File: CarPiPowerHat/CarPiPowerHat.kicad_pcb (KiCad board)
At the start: 4 copper layers, 65 x 56 mm, 18 parts, among them J3 40HAT, J6 CONN_02X02, J9 CONN_01X02, Q1 DMG2305UX, Q2 DMMT5401, U2 CAT24C32

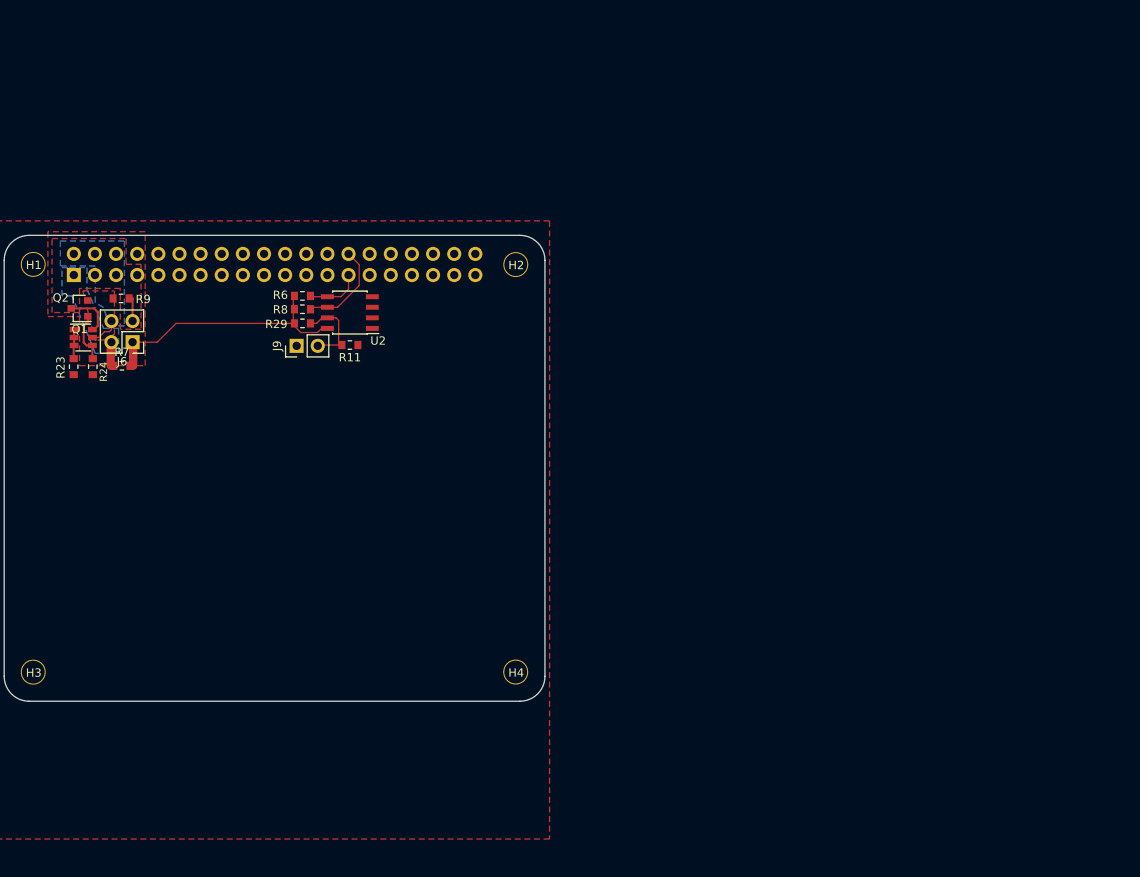
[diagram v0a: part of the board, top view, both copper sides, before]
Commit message: Added first firmware version
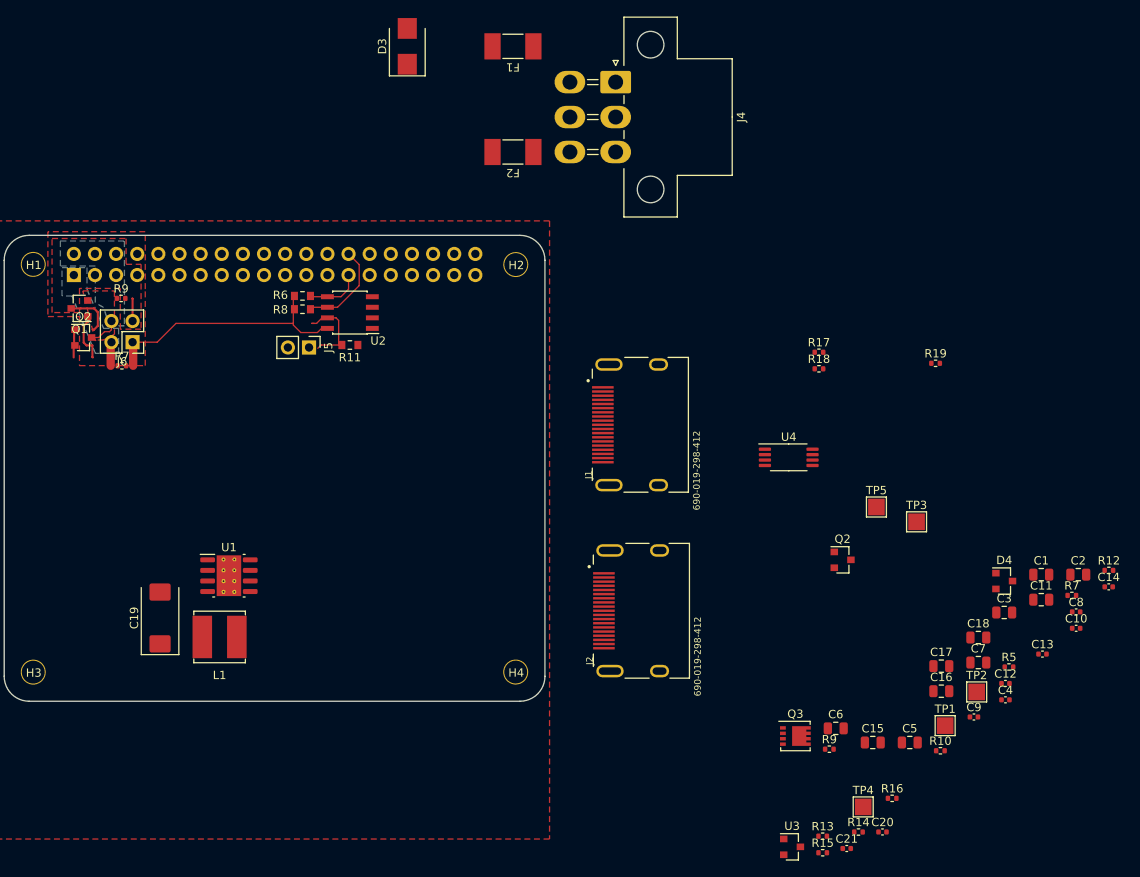
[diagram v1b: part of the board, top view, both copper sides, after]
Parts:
- removed J9: CONN_01X02, Connector_PinHeader_2.54mm:PinHeader_1x02_P2.54mm_Vertical
- removed R23, R29: 10K, Resistor_SMD:R_0603_1608Metric_Pad0.84x1.00mm_HandSolder
- removed R24: 47K, Resistor_SMD:R_0603_1608Metric_Pad0.84x1.00mm_HandSolder
- added C1: 10u 35v, Capacitor_SMD:C_0805_2012Metric, F.Cu at (203.2, 101.6)
- added C10: 100n, Capacitor_SMD:C_0402_1005Metric, F.Cu at (207.4, 108.0)
- added C11: 10u 35v, Capacitor_SMD:C_0805_2012Metric, F.Cu at (203.2, 104.6)
- added C12: nf, Capacitor_SMD:C_0402_1005Metric, F.Cu at (198.9, 114.7)
- added C13: 1.2nF, Capacitor_SMD:C_0402_1005Metric, F.Cu at (203.3, 111.2)
- added C14: nf, Capacitor_SMD:C_0402_1005Metric, F.Cu at (211.3, 103.1)
- added C15: 10u, Capacitor_SMD:C_0805_2012Metric, F.Cu at (182.9, 121.8)
- added C16: 10u, Capacitor_SMD:C_0805_2012Metric, F.Cu at (191.2, 115.6)
- added C17: 10u, Capacitor_SMD:C_0805_2012Metric, F.Cu at (191.2, 112.6)
- added C18: 10u, Capacitor_SMD:C_0805_2012Metric, F.Cu at (195.6, 109.2)
- added C19: 100uF, Capacitor_Tantalum_SMD:CP_EIA-7343-31_Kemet-D, F.Cu at (97.3, 106.8)
- added C2: 10u 35v, Capacitor_SMD:C_0805_2012Metric, F.Cu at (207.7, 101.6)
- added C20: 100n, Capacitor_SMD:C_0402_1005Metric, F.Cu at (184.1, 132.5)
- added C21: 100n, Capacitor_SMD:C_0402_1005Metric, F.Cu at (179.8, 134.5)
- added C3: 10u 35v, Capacitor_SMD:C_0805_2012Metric, F.Cu at (198.8, 106.2)
- added C4: 100n 100v, Capacitor_SMD:C_0402_1005Metric, F.Cu at (198.9, 116.7)
- added C5: 10u 35v, Capacitor_SMD:C_0805_2012Metric, F.Cu at (187.4, 121.8)
- added C6: 10u 35v, Capacitor_SMD:C_0805_2012Metric, F.Cu at (178.5, 120.1)
- added C7: 10u 35v, Capacitor_SMD:C_0805_2012Metric, F.Cu at (195.6, 112.2)
- added C8: 100n, Capacitor_SMD:C_0402_1005Metric, F.Cu at (207.4, 106.1)
- added C9: 100n, Capacitor_SMD:C_0402_1005Metric, F.Cu at (195.1, 118.7)
- added D3: D_TVS, Diode_SMD:D_SMB, F.Cu at (127.0, 38.1)
- added D4: MMBZ5242BLT3G, Diode_SMD:D_SOT-23_ANK, F.Cu at (198.8, 102.4)
- added F1: Fuse, Fuse:Fuse_Littelfuse-NANO2-451_453, F.Cu at (139.7, 38.1)
- added F2: Fuse, Fuse:Fuse_Littelfuse-NANO2-451_453, F.Cu at (139.7, 50.8)
- added J1: 690-019-298-412, project_footprints:EDAC 690-019-298-412, F.Cu at (151.2, 83.6)
- added J2: 690-019-298-412, project_footprints:EDAC 690-019-298-412, F.Cu at (151.4, 105.9)
- added J4: Conn_02x03_Counter_Clockwise, Connector_Molex:Molex_Mini-Fit_Jr_5569-06A1_2x03_P4.20mm_Horizontal, F.Cu at (152.0, 42.4)
- added J5: CONN_01X02, Connector_PinHeader_2.54mm:PinHeader_1x02_P2.54mm_Vertical, F.Cu at (115.2, 74.3)
- added L1: SRN6045TA-3R3Y, Inductor_SMD:L_Bourns_SRN6045TA, F.Cu at (104.4, 109.1)
- added Q2: DMG2305UX, Package_TO_SOT_SMD:SOT-23, F.Cu at (179.3, 99.8)
- added Q3: DMP3013SFV-7, Package_SON:Diodes_PowerDI3333-8, F.Cu at (173.7, 121.0)
- added R10: 12K 1%, Resistor_SMD:R_0402_1005Metric, F.Cu at (191.1, 122.8)
- added R12: 2.2K 1%, Resistor_SMD:R_0402_1005Metric, F.Cu at (211.3, 101.1)
- added R13: 10K 1%, Resistor_SMD:R_0402_1005Metric, F.Cu at (176.9, 133.0)
- added R14: 10K 1%, Resistor_SMD:R_0402_1005Metric, F.Cu at (181.2, 132.5)
- added R15: 10K 1%, Resistor_SMD:R_0402_1005Metric, F.Cu at (176.9, 135.0)
- added R16: 10K 1%, Resistor_SMD:R_0402_1005Metric, F.Cu at (185.3, 128.5)
- added R17: 10K 1%, Resistor_SMD:R_0402_1005Metric, F.Cu at (176.5, 74.9)
- added R18: 320 1%, Resistor_SMD:R_0402_1005Metric, F.Cu at (176.5, 76.9)
- added R19: 3.3K 1%, Resistor_SMD:R_0402_1005Metric, F.Cu at (190.5, 76.2)
- added R5: 12K 1%, Resistor_SMD:R_0402_1005Metric, F.Cu at (199.3, 112.7)
- added R7: 10R, Resistor_SMD:R_0402_1005Metric, F.Cu at (206.9, 104.1)
- added R9: 20K 1%, Resistor_SMD:R_0402_1005Metric, F.Cu at (177.7, 122.6)
- added TP1: TestPoint, TestPoint:TestPoint_Pad_2.0x2.0mm, F.Cu at (191.7, 119.8)
- added TP2: TestPoint, TestPoint:TestPoint_Pad_2.0x2.0mm, F.Cu at (195.4, 115.7)
- added TP3: TestPoint, TestPoint:TestPoint_Pad_2.0x2.0mm, F.Cu at (188.2, 95.2)
- added TP4: TestPoint, TestPoint:TestPoint_Pad_2.0x2.0mm, F.Cu at (181.8, 129.5)
- added TP5: TestPoint, TestPoint:TestPoint_Pad_2.0x2.0mm, F.Cu at (183.4, 93.5)
- added U1: AP64501SP-13, Package_SO:SOIC-8-1EP_3.9x4.9mm_P1.27mm_EP2.95x4.9mm_Mask2.71x3.4mm_ThermalVias, F.Cu at (105.6, 101.7)
- added U3: LM3480-5.0, Package_TO_SOT_SMD:SOT-23, F.Cu at (173.2, 134.3)
- added U4: ATtiny45V-10X, Package_SO:TSSOP-8_4.4x3mm_P0.65mm, F.Cu at (172.8, 87.5)
- J6: value CONN_02X02 -> Conn_01x15_Female
- Q1: value DMG2305UX -> DMMT5401
- Q2: value DMMT5401 -> DMG2305UX; footprint Package_TO_SOT_SMD:SOT-23-6 -> Package_TO_SOT_SMD:SOT-23
- R11: value DNP -> 130
- R7: value DNP -> 10R; footprint Resistor_SMD:R_0603_1608Metric_Pad0.84x1.00mm_HandSolder -> Resistor_SMD:R_0402_1005Metric
- R9: value DNP -> 20K 1%; footprint Resistor_SMD:R_0603_1608Metric_Pad0.84x1.00mm_HandSolder -> Resistor_SMD:R_0402_1005Metric
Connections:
- J3 pad 1: /P3V3_HAT -> /+3.3v
- J3 pad 16: unconnected-(J3-Pad16) -> PWR_SENSE_OUT
- J3 pad 17: unconnected-(J3-Pad17) -> /+3.3v
- J3 pad 18: unconnected-(J3-Pad18) -> PWR_SENSE_IN
- J3 pad 22: unconnected-(J3-Pad22) -> REVERSE_SENSE
- J3 pad 24: unconnected-(J3-Pad24) -> LIGHT_SENSE
- J6 pad 1: /P3V3 -> Net-(J1-Pad15)
- J6 pad 2: /P3V3_HAT -> Net-(J1-Pad14)
- J6 pad 3: /P5V -> Net-(J1-Pad13)
- J6 pad 4: /P5V_HAT -> Net-(J1-Pad1)
- Q1 pad 2: /P5V_HAT -> Net-(Q1-Pad1)
- Q1 pad 3: /P5V -> Net-(Q1-Pad1)
- Q2 pad 1: Net-(Q2-Pad1) -> Net-(Q1-Pad4)
- Q2 pad 2: Net-(Q2-Pad1) -> /P5V_HAT
- Q2 pad 3: Net-(Q2-Pad1) -> /PSU/P5V
- R11 pad 1: Net-(J9-Pad2) -> Net-(D1-Pad1)
- R7 pad 1: /P3V3_HAT -> Net-(L1-Pad1)
- R7 pad 2: /P3V3 -> Net-(C8-Pad1)
- R9 pad 1: /P5V_HAT -> Net-(C12-Pad1)
- R9 pad 2: /P5V -> Net-(C13-Pad1)
- U2 pad 7: Net-(J9-Pad2) -> Net-(J5-Pad2)
- U2 pad 8: /P3V3 -> /+3.3v
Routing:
- net Net-(J9-Pad2): track 9.58 -> 0.00 mm
- net Net-(D1-Pad1): track 0.00 -> 9.58 mm
- net /P5V: track 8.71 -> 0.00 mm
- net Net-(Q1-Pad1): track 6.02 -> 12.0 mm
- net /P5V_HAT: track 3.77 -> 0.00 mm
- net Net-(J1-Pad1): track 0.00 -> 3.72 mm
- net Net-(Q2-Pad1): track 3.37 -> 0.00 mm
- net Net-(C21-Pad1): track 0.00 -> 3.37 mm
- net Net-(J1-Pad14): track 0.00 -> 2.88 mm
- net /P3V3_HAT: track 2.88 -> 0.00 mm
- net Net-(J1-Pad13): track 0.00 -> 2.73 mm
- added copper zone on B.Cu, net /+3.3v
- added copper zone on F.Cu, net Net-(C13-Pad1)
- removed copper zone on B.Cu, net /P3V3_HAT
- removed copper zone on F.Cu, net /P5V
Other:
- board text removed: "This is a HAT compatible PCB starting design based on the official Raspberry Pi specs at: https://github.com/raspberrypi/hats/blob/master/designguide.md Currently the camera slot and display cutout are not here. See the schematic for the details on the EEPROM and power setup. This board does have the correct components for powering the Pi via the HAT. If you need the Pi to provide 5V or 3.3V, ple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"

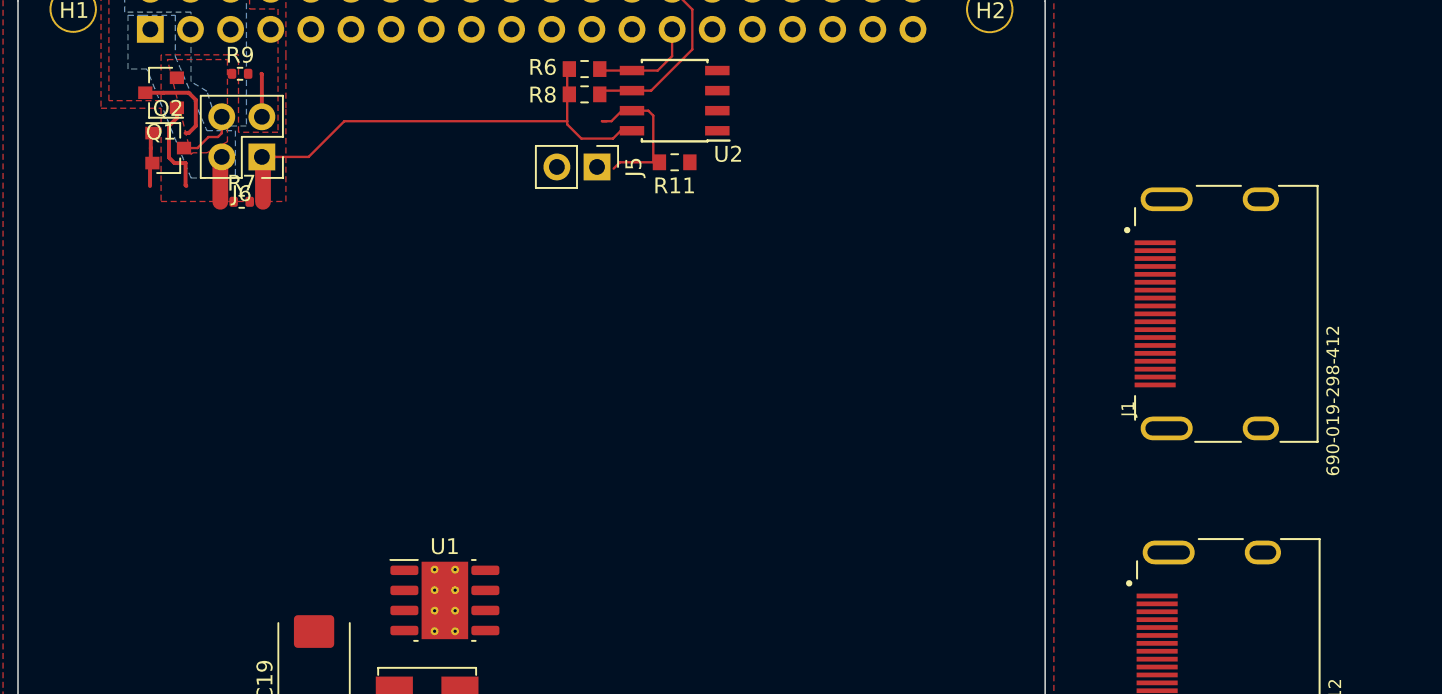
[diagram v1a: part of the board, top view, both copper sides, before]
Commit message: added connectors
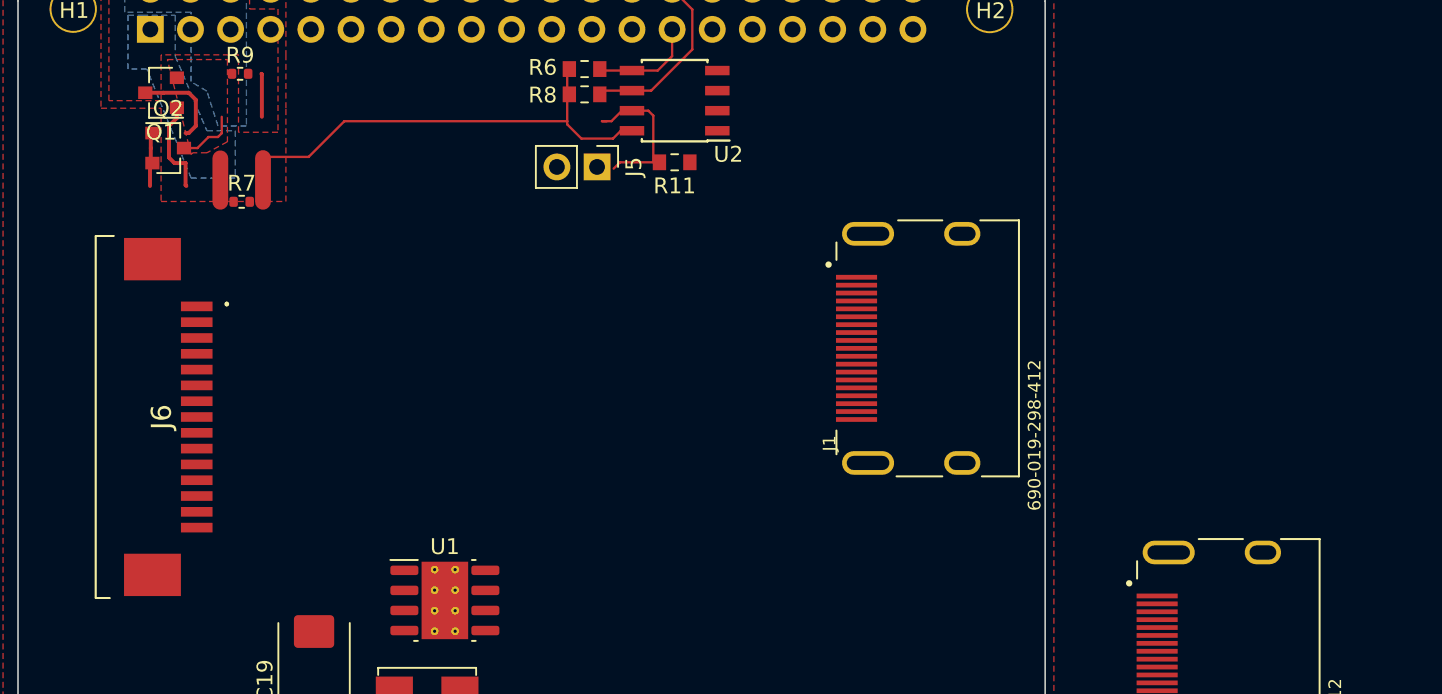
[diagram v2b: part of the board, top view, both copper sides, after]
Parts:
- J6: value Conn_01x15_Female -> 1-84953-5; footprint Connector_PinHeader_2.54mm:PinHeader_2x02_P2.54mm_Vertical -> project_footprints:1849535
- moved J1 19.0 mm to (132.3, 85.8)
- moved J6 18.2 mm to (86.2, 90.1), turned to -90 degrees
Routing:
- net Net-(J1-Pad1): track 3.72 -> 0.00 mm
- net /PSU/P5V: track 0.00 -> 3.72 mm

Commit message: doing some traces
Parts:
- removed the Q2 at (179.3, 99.8)
- removed the R7 at (206.9, 104.1)
- removed the R9 at (177.7, 122.6)
- added BT1: Battery_Cell, Battery:BatteryHolder_Keystone_3034_1x20mm, F.Cu at (88.4, 58.2)
- added C1: 0.1uF, Adafruit I2S Audio UDA1334 Bonnet:0603-NO, F.Cu at (51.8, 100.4)
- added C11: 10uF, Adafruit I2S Audio UDA1334 Bonnet:0805-NO, F.Cu at (29.0, 86.7)
- added C13: 10uF, Adafruit I2S Audio UDA1334 Bonnet:0805-NO, F.Cu at (29.9, 92.9)
- added C14: 10uF, Adafruit I2S Audio UDA1334 Bonnet:0805-NO, F.Cu at (51.3, 89.6)
- added C2: 0.1uF, Adafruit I2S Audio UDA1334 Bonnet:0603-NO, F.Cu at (51.3, 91.4)
- added C22: 10u, Resistor_SMD:R_0603_1608Metric, F.Cu at (171.3, -1.14)
- added C23: 10u, Resistor_SMD:R_0603_1608Metric, F.Cu at (171.3, 16.7)
- added C24: 100n, Capacitor_SMD:C_0402_1005Metric, F.Cu at (88.6, 37.5)
- added C25: 100n, Capacitor_SMD:C_0402_1005Metric, F.Cu at (18.0, 95.3)
- added C26: 100n, Capacitor_SMD:C_0402_1005Metric, F.Cu at (18.0, 93.3)
- added C3: 0.1uF, Adafruit I2S Audio UDA1334 Bonnet:0603-NO, F.Cu at (55.7, 87.1)
- added C4: 47uF, Adafruit I2S Audio UDA1334 Bonnet:PANASONIC_C, F.Cu at (45.9, 99.5)
- added C5: 10uF, Adafruit I2S Audio UDA1334 Bonnet:0805-NO, F.Cu at (50.3, 100.4)
- added C6: 47uF, Adafruit I2S Audio UDA1334 Bonnet:PANASONIC_C, F.Cu at (46.6, 90.5)
- added C7: 0.01uF, Adafruit I2S Audio UDA1334 Bonnet:0603-NO, F.Cu at (39.7, 88.7)
- added C8: 0.01uF, Adafruit I2S Audio UDA1334 Bonnet:0603-NO, F.Cu at (42.2, 99.5)
- added D1: LED, LED_SMD:LED_0603_1608Metric, F.Cu at (98.5, 115.4)
- added D10: D, Diode_SMD:D_SOD-123F, F.Cu at (174.2, -4.79)
- added D12: D_Schottky, Diode_SMD:D_SOD-123, F.Cu at (174.2, 7.37)
- added D13: D_Schottky, Diode_SMD:D_SOD-123, F.Cu at (170.9, 7.37)
- added D14: D, Diode_SMD:D_SOD-123F, F.Cu at (174.2, 13.0)
- added D15: BAT54C-7-F, Package_TO_SOT_SMD:SOT-23, F.Cu at (91.4, 40.7)
- added D2: LED, LED_SMD:LED_0603_1608Metric, F.Cu at (102.5, 115.4)
- added D6: D_Dual_CommonCathode_AAK_Parallel, Package_TO_SOT_SMD:SOT-23, F.Cu at (150.9, 60.8)
- added D8: D_Schottky, Diode_SMD:D_SOD-123, F.Cu at (174.2, -10.4)
- added D9: D_Schottky, Diode_SMD:D_SOD-123, F.Cu at (170.9, -10.4)
- added FB1: Ferrite, Adafruit I2S Audio UDA1334 Bonnet:0805, F.Cu at (33.4, 91.3)
- added FB2: Ferrite, Adafruit I2S Audio UDA1334 Bonnet:0805, F.Cu at (34.3, 88.2)
- added FB2: FerriteBead, Resistor_SMD:R_0805_2012Metric, F.Cu at (171.1, -5.35)
- added FB3: FerriteBead, Resistor_SMD:R_0805_2012Metric, F.Cu at (171.1, 12.4)
- added H5: 3mm_Mounting_Hole, MountingHole:MountingHole_2.7mm_M2.5, F.Cu at (170.5, 113.0)
- added H6: 3mm_Mounting_Hole, MountingHole:MountingHole_2.7mm_M2.5, F.Cu at (170.5, 35.0)
- added J7: HDMI_A_1.4, project_footprints:EDAC 690-019-298-412, F.Cu at (113.0, 107.0)
- added J8: AudioJack2_Ground, Connector_Audio:Jack_3.5mm_CUI_SJ-3524-SMT_Horizontal, F.Cu at (127.6, 110.4)
- added Q1: DMG2305, Adafruit I2S Audio UDA1334 Bonnet:SOT23-WIDE, F.Cu at (55.7, 90.7)
- added R1: 10K, Adafruit I2S Audio UDA1334 Bonnet:0603-NO, F.Cu at (56.9, 93.4)
- added R1: 10K, Resistor_SMD:R_0402_1005Metric_Pad0.72x0.64mm_HandSolder, F.Cu at (137.7, 34.1)
- added R2: 10K, Adafruit I2S Audio UDA1334 Bonnet:0603-NO, F.Cu at (55.7, 88.3)
- added R2: DNP, project_footprints:R_0603_1608Metric_Pad0.84x1.00mm_HandSolder, F.Cu at (137.8, 66.9)
- added R20: 200, Resistor_SMD:R_0402_1005Metric, F.Cu at (174.9, -0.62)
- added R21: 200, Resistor_SMD:R_0402_1005Metric, F.Cu at (174.9, 17.2)
- added R3: 220k, Adafruit I2S Audio UDA1334 Bonnet:0603-NO, F.Cu at (42.2, 87.8)
- added R3: 10K, project_footprints:R_0603_1608Metric_Pad0.84x1.00mm_HandSolder, F.Cu at (138.0, 77.4)
- added R4: 47K, Resistor_SMD:R_0402_1005Metric_Pad0.72x0.64mm_HandSolder, F.Cu at (135.5, 34.1)
- added R4: 100, Adafruit I2S Audio UDA1334 Bonnet:0603-NO, F.Cu at (42.1, 89.6)
- added R5: 220k, Adafruit I2S Audio UDA1334 Bonnet:0603-NO, F.Cu at (48.7, 104.1)
- added R6: 100, Adafruit I2S Audio UDA1334 Bonnet:0603-NO, F.Cu at (45.5, 104.1)
- added U1: UDA1334ATS, Adafruit I2S Audio UDA1334 Bonnet:SSOP16_4.4MM, F.Cu at (52.2, 95.3)
- added U2: AP2112-3.3K, Adafruit I2S Audio UDA1334 Bonnet:SOT23-5, F.Cu at (29.7, 89.7)
- added U5: PCF85063AT/AAZ, Package_SO:SOIC-8_3.9x4.9mm_P1.27mm, F.Cu at (85.7, 41.7)
- added U6: RT9742SNGV, Package_TO_SOT_SMD:SOT-23, F.Cu at (14.3, 94.6)
- added U8: UDA1334ATS, Package_SO:SSOP-16_4.4x5.2mm_P0.65mm, F.Cu at (18.4, 101.1)
- added X2: 19269, Adafruit I2S Audio UDA1334 Bonnet:4UCONN_19269, F.Cu at (38.3, 105.4)
- added Y1: X32K768S301, Crystal:Crystal_SMD_3215-2Pin_3.2x1.5mm, F.Cu at (80.6, 41.0)
- H1, H2, H3, H4: footprint project_footprints:NPTH_3mm_ID -> MountingHole:MountingHole_2.7mm_M2.5
- J1: value 690-019-298-412 -> HDMI_A_1.4
- J2: value 690-019-298-412 -> 1-84953-5; footprint project_footprints:EDAC 690-019-298-412 -> project_footprints:1849535
- J5: value CONN_01X02 -> USB_A; footprint Connector_PinHeader_2.54mm:PinHeader_1x02_P2.54mm_Vertical -> Connector_USB:USB_A_Wuerth_614004134726_Horizontal
- J6, TP1, TP2, TP3, TP4, TP5: moved to B.Cu
- Q1: footprint Package_TO_SOT_SMD:SOT-23 -> project_footprints:SOT26
- R11: footprint Resistor_SMD:R_0603_1608Metric_Pad0.84x1.00mm_HandSolder -> Resistor_SMD:R_0402_1005Metric
- R6, R8: footprint Resistor_SMD:R_0603_1608Metric_Pad0.84x1.00mm_HandSolder -> project_footprints:R_0603_1608Metric_Pad0.84x1.00mm_HandSolder
- moved U3 152.2 mm to (151.0, -16.2), turned to -90 degrees
- moved R15 150.0 mm to (150.3, -12.6), turned to -90 degrees
- moved R13 147.7 mm to (152.3, -12.6), turned to -90 degrees
- moved C21 147.1 mm to (150.8, -9.68), turned to -90 degrees
- moved R14 143.7 mm to (152.8, -8.27), turned to -90 degrees
- moved C20 141.4 mm to (152.8, -5.38), turned to -90 degrees
- moved R16 135.7 mm to (156.8, -4.22), turned to -90 degrees
- moved TP3 93.6 mm to (126.2, 25.1), turned to -90 degrees
- moved R17 89.7 mm to (163.7, -13.9), turned to -90 degrees
- moved R18 81.8 mm to (103.3, 113.4), turned to -90 degrees
- moved R19 81.1 mm to (162.4, 0.08), turned to -90 degrees
- moved TP4 80.9 mm to (144.1, 57.9), turned to -90 degrees
- moved J2 79.6 mm to (106.0, 40.5), turned to 180 degrees
- moved H3 78.3 mm to (81.5, 35.0), turned to -90 degrees
- moved D3 77.6 mm to (168.1, 103.9)
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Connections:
- net /HDMI Connectors/A renamed /HDMI Connector Camera/A
- net /HDMI Connectors/B renamed /HDMI Connector Camera/B
- net /HDMI Connectors/C renamed /HDMI Connector Camera/C
- net /HDMI Connectors/D renamed /HDMI Connector Camera/D
- net Net-(J1-Pad1) renamed /HDMI Connector Camera/D2+
- net Net-(J1-Pad10) renamed /HDMI Connector Camera/CK+
- net Net-(J1-Pad12) renamed /HDMI Connector Camera/CK-
- net Net-(J1-Pad13) renamed /HDMI Connector Camera/CEC
- net Net-(J1-Pad14) renamed /HDMI Connector Camera/UTILITY/HEAC+
- net Net-(J1-Pad15) renamed /HDMI Connector Camera/C_SCL
- net Net-(J1-Pad3) renamed /HDMI Connector Camera/D2-
- net Net-(J1-Pad4) renamed /HDMI Connector Camera/D1-
- net Net-(J1-Pad6) renamed /HDMI Connector Camera/D1+
- net Net-(J1-Pad7) renamed /HDMI Connector Camera/D0+
- net Net-(J1-Pad9) renamed /HDMI Connector Camera/D0-
- J1 pad SH1: /HDMI Connectors/xGND -> GND
- J1 pad SH2: /HDMI Connectors/xGND -> GND
- J1 pad SH3: /HDMI Connectors/xGND -> GND
- J1 pad SH4: /HDMI Connectors/xGND -> GND
- J2 pad 1: /HDMI Connectors/HDMI1_D2_P -> /HDMI Connector Display/C_SCL
- J2 pad 10: /HDMI Connectors/HDMI1_CK_P -> /HDMI Connector Display/D0+
- J2 pad 11: GND -> /HDMI Connector Display/D0-
- J2 pad 12: /HDMI Connectors/HDMI1_CK_N -> GND
- J2 pad 13: /HDMI Connectors/HDMI1_CEC -> /HDMI Connector Display/CK+
- J2 pad 14: unconnected-(J2-Pad14) -> /HDMI Connector Display/CK-
- J2 pad 15: /HDMI Connectors/HDMI1_SCL -> GND
- J2 pad 2: GND -> /HDMI Connector Display/UTILITY/HEAC+
- J2 pad 3: /HDMI Connectors/HDMI1_D2_N -> /HDMI Connector Display/CEC
- J2 pad 4: /HDMI Connectors/HDMI1_D1_P -> /HDMI Connector Display/D2+
- J2 pad 5: GND -> /HDMI Connector Display/D2-
- J2 pad 6: /HDMI Connectors/HDMI1_D1_N -> GND
- J2 pad 7: /HDMI Connectors/HDMI1_D0_P -> /HDMI Connector Display/D1-
- J2 pad 8: GND -> /HDMI Connector Display/D1+
- J2 pad 9: /HDMI Connectors/HDMI1_D0_N -> GND
- J3 pad 12: unconnected-(J3-Pad12) -> /BITCLK
- J3 pad 3: unconnected-(J3-Pad3) -> /SDA
- J3 pad 35: unconnected-(J3-Pad35) -> /LRCLK
- J3 pad 36: unconnected-(J3-Pad36) -> /BCM16
- J3 pad 40: unconnected-(J3-Pad40) -> /DATAIN
- J3 pad 5: unconnected-(J3-Pad5) -> /SCL
- J4 pad 2: CAR_REVERSE -> CAR_IGN
- J4 pad 5: CAR_IGN -> CAR_REVERSE
- J5 pad 1: GND -> /PSU/USB_5v
- J5 pad 2: Net-(J5-Pad2) -> unconnected-(J5-Pad2)
- R6 pad 1: /P3V3 -> /+3.3v
- R8 pad 1: /P3V3 -> /+3.3v
- U2 pad 7: Net-(J5-Pad2) -> Net-(R2-Pad1)
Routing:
- net (no net): track 0.00 -> 206.0 mm, vias 0 -> 8
- net /HDMI Connector Display/CK-: track 0.00 -> 73.7 mm
- net /HDMI Connector Display/CK+: track 0.00 -> 72.1 mm
- net /HDMI Connector Display/D1+: track 0.00 -> 72.1 mm
- net /HDMI Connector Display/D1-: track 0.00 -> 72.0 mm
- net /HDMI Connector Display/D0+: track 0.00 -> 72.0 mm
- net /HDMI Connector Display/D0-: track 0.00 -> 72.0 mm
- net /HDMI Connector Display/D2-: track 0.00 -> 72.0 mm
- net /HDMI Connector Display/D2+: track 0.00 -> 71.9 mm
- net /HDMI Connector Display/C_SCL: track 0.00 -> 68.3 mm, vias 0 -> 2
- net /HDMI Connector Display/UTILITY/HEAC+: track 0.00 -> 67.5 mm, vias 0 -> 2
- net /HDMI Connector Display/CEC: track 0.00 -> 66.7 mm, vias 0 -> 2
- net GND: track 0.00 -> 60.8 mm, vias 0 -> 25
- net /P3V3: track 31.3 -> 0.00 mm
- net /HDMI Connector Camera/D2+: track 0.00 -> 11.8 mm, vias 0 -> 1
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- added copper zone on B.Cu, net AGND
- added copper zone on In1.Cu, net AGND
- removed copper zone on B.Cu, net /+3.3v
- removed copper zone on B.Cu, net /P5V_HAT
- removed copper zone on F.Cu, net GND
- removed copper zone on F.Cu, net Net-(C13-Pad1)
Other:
- board size 65 x 56 mm -> 96 x 85 mm
